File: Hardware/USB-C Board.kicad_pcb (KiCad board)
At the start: 2 copper layers, 34 x 34 mm, 52 parts, among them J1 USB_C_Receptacle_USB2.0, J2 Conn_01x04_Male, J3 Conn_01x02_Male, J4 Conn_01x02_Male, J5 Conn_01x02_Male, J9 Conn_01x04_MountingPin, Q1 DMP3013SFV, SW1 SW_Push, U1 AMS1117-3.3, U3 STUSB4500QTR

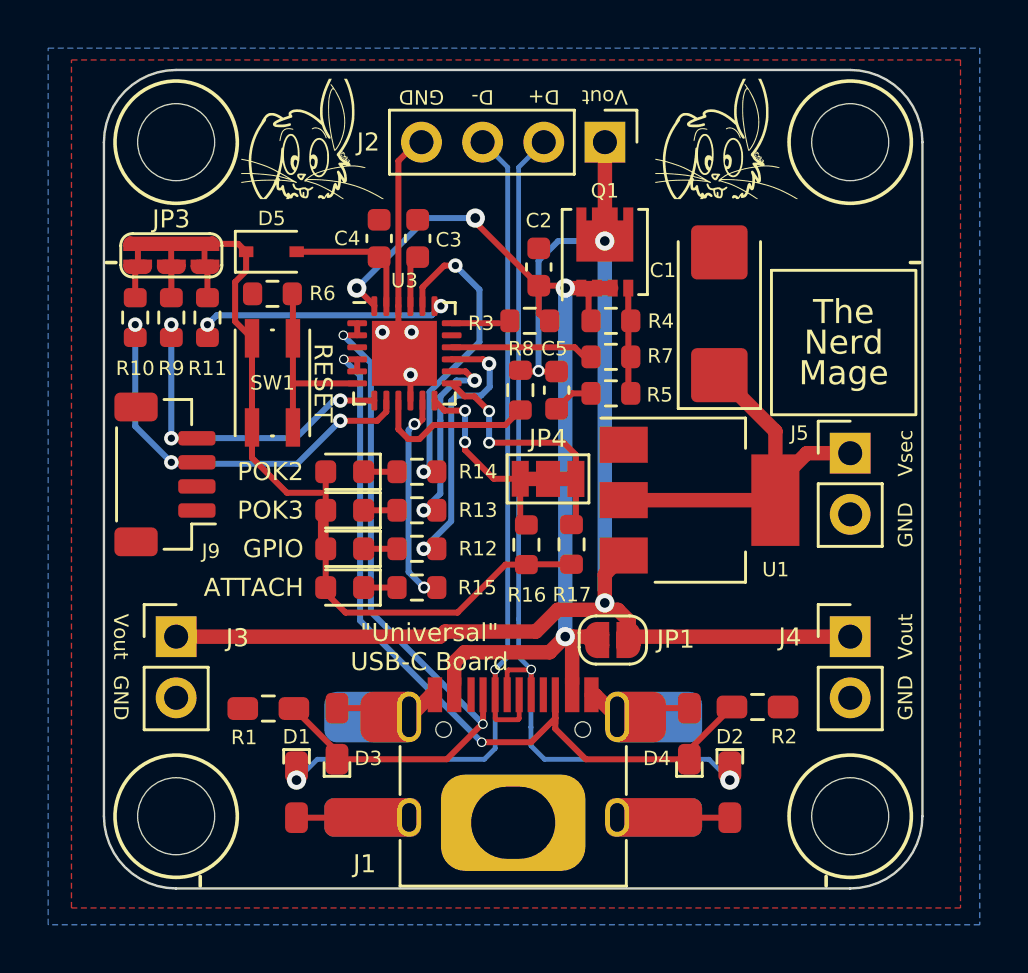
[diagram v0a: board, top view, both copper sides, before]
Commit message: tweakin' header positions
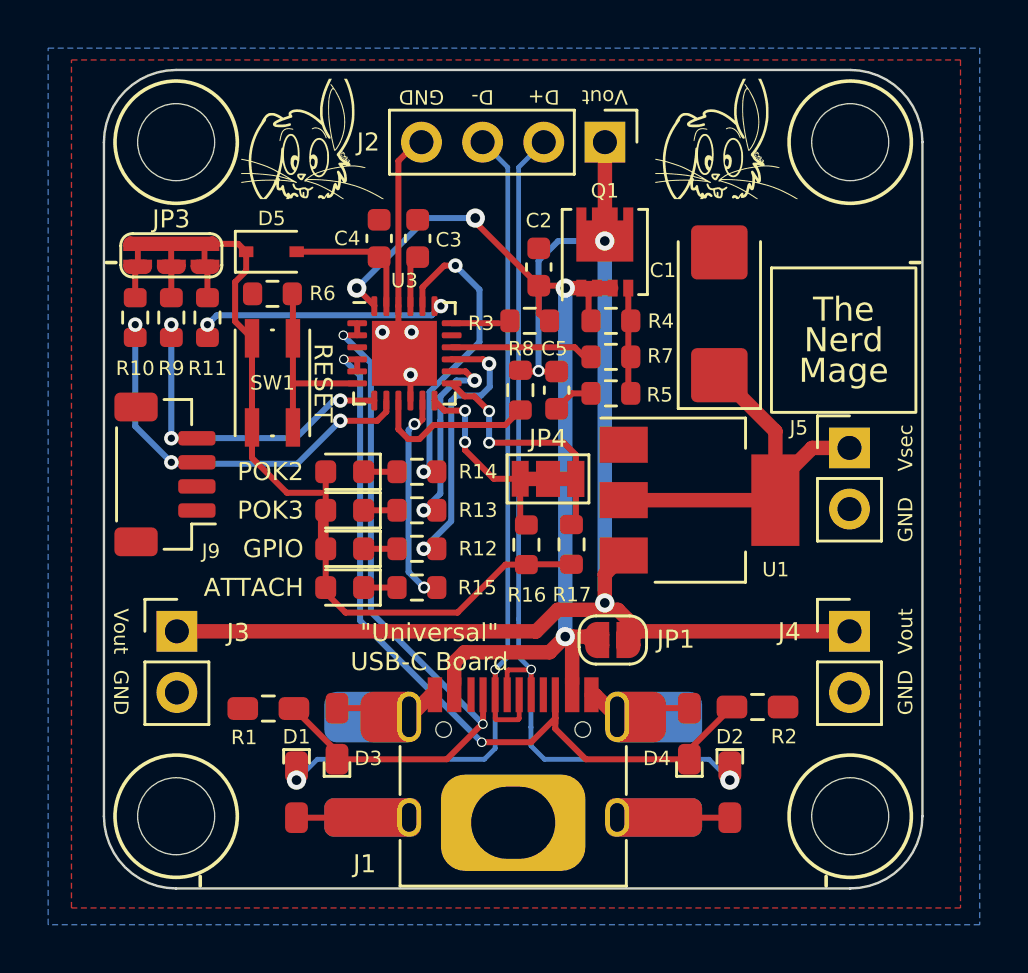
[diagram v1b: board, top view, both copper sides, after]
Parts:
- moved J3 0.22 mm to (86.0, 93.3)
- moved J4 0.22 mm to (114.0, 93.3)
- moved J5 0.22 mm to (114.0, 85.7)
- moved REF** 0.10 mm to (113.7, 81.2)
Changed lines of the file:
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@@
   )
   (footprint "Connector_PinHeader_2.54mm:PinHeader_1x02_P2.54mm_Vertical" (layer "F.Cu")
-    (at 114 93.54)
+    (at 113.97 93.32)
     (descr "Through hole straight pin header, 1x02, 2.54mm pitch, single row")
     (tags "Through hole pin header THT 1x02 2.54mm single row")
@@
   )
   (footprint "Tinker:NerdMage" (layer "F.Cu")
-    (at 113.729274 81.323075)
+    (at 113.729274 81.223075)
     (attr smd)
     (fp_text reference "REF**" (at 0 -0.5 unlocked) (layer "F.SilkS") hide
@@
   )
   (footprint "Connector_PinHeader_2.54mm:PinHeader_1x02_P2.54mm_Vertical" (layer "F.Cu")
-    (at 86 93.54)
+    (at 86.03 93.32)
     (descr "Through hole straight pin header, 1x02, 2.54mm pitch, single row")
     (tags "Through hole pin header THT 1x02 2.54mm single row")
@@
   )
   (footprint "Connector_PinHeader_2.54mm:PinHeader_1x02_P2.54mm_Vertical" (layer "F.Cu")
-    (at 114 85.92)
+    (at 113.97 85.7)
     (descr "Through hole straight pin header, 1x02, 2.54mm pitch, single row")
     (tags "Through hole pin header THT 1x02 2.54mm single row")
@@
     (effects (font (size 0.6 0.6) (thickness 0.15)) (justify mirror))
   )
-  (gr_text "GND" (at 116.3 88.9 90) (layer "B.SilkS")
+  (gr_text "GND" (at 116.3 88.68 90) (layer "B.SilkS")
     (effects (font (size 0.6 0.6) (thickness 0.125)) (justify mirror))
   )
-  (gr_text "GND" (at 83.7 96.08 270) (layer "B.SilkS")
+  (gr_text "GND" (at 83.7 95.86 270) (layer "B.SilkS")
     (effects (font (size 0.6 0.6) (thickness 0.125)) (justify mirror))
   )
-  (gr_text "Vout" (at 116.3 93.54 90) (layer "B.SilkS")
+  (gr_text "Vout" (at 116.3 93.32 90) (layer "B.SilkS")
     (effects (font (size 0.6 0.6) (thickness 0.125)) (justify mirror))
   )
@@
     (effects (font (size 0.6 0.6) (thickness 0.125)) (justify mirror))
   )
-  (gr_text "Vsec" (at 116.3 85.92 90) (layer "B.SilkS")
+  (gr_text "Vsec" (at 116.3 85.7 90) (layer "B.SilkS")
     (effects (font (size 0.6 0.6) (thickness 0.125)) (justify mirror))
   )
-  (gr_text "GND" (at 116.3 96.08 90) (layer "B.SilkS")
+  (gr_text "GND" (at 116.3 95.86 90) (layer "B.SilkS")
     (effects (font (size 0.6 0.6) (thickness 0.125)) (justify mirror))
   )
@@
     (effects (font (size 1 1) (thickness 0.15)) (justify mirror))
   )
-  (gr_text "Vout" (at 83.7 93.54 270) (layer "B.SilkS")
+  (gr_text "Vout" (at 83.7 93.32 270) (layer "B.SilkS")
     (effects (font (size 0.6 0.6) (thickness 0.125)) (justify mirror))
   )
@@
     (effects (font (size 0.6 0.6) (thickness 0.125)) (justify mirror))
   )
-  (gr_text "Vout" (at 116.3 93.54 90) (layer "F.SilkS")
+  (gr_text "Vout" (at 116.3 93.32 90) (layer "F.SilkS")
     (effects (font (size 0.6 0.6) (thickness 0.125)))
   )
@@
     (effects (font (size 0.6 0.6) (thickness 0.15)))
   )
-  (gr_text "GND" (at 116.3 88.9 90) (layer "F.SilkS")
+  (gr_text "GND" (at 116.3 88.68 90) (layer "F.SilkS")
     (effects (font (size 0.6 0.6) (thickness 0.125)))
   )
@@
     (effects (font (size 0.75 0.75) (thickness 0.15)) (justify right))
   )
-  (gr_text "GND" (at 116.3 96.08 90) (layer "F.SilkS")
+  (gr_text "GND" (at 116.3 95.86 90) (layer "F.SilkS")
     (effects (font (size 0.6 0.6) (thickness 0.125)))
   )
@@
     (effects (font (size 0.75 0.75) (thickness 0.15)) (justify right))
   )
-  (gr_text "GND" (at 83.7 96.08 270) (layer "F.SilkS")
+  (gr_text "GND" (at 83.7 95.86 270) (layer "F.SilkS")
     (effects (font (size 0.6 0.6) (thickness 0.125)))
   )
@@
     (effects (font (size 0.6 0.6) (thickness 0.125)))
   )
-  (gr_text "Vsec" (at 116.3 85.92 90) (layer "F.SilkS")
+  (gr_text "Vsec" (at 116.3 85.7 90) (layer "F.SilkS")
     (effects (font (size 0.6 0.6) (thickness 0.125)))
   )
-  (gr_text "Vout" (at 83.7 93.54 270) (layer "F.SilkS")
+  (gr_text "Vout" (at 83.7 93.32 270) (layer "F.SilkS")
     (effects (font (size 0.6 0.6) (thickness 0.125)))
   )
@@
   (segment (start 87.3 79.460136) (end 87.3 78.28) (width 0.25) (layer "F.Cu") (net 25))
   (segment (start 87.3 78.28) (end 87.2 78.18) (width 0.25) (layer "F.Cu") (net 25))
+  (segment (start 100.94 93.32) (end 100.947498 93.327498) (width 0.6) (layer "F.Cu") (net 26))
+  (segment (start 86 93.32) (end 100.94 93.32) (width 0.6) (layer "F.Cu") (net 26))
   (segment (start 101.849483 92.425514) (end 104.348538 92.425514) (width 0.6) (layer "F.Cu") (net 26))
   (segment (start 103.81 77.101582) (end 103.805361 77.106221) (width 0.6) (layer "F.Cu") (net 26))
   (segment (start 103.805361 92.14) (end 103.805361 90.956371) (width 0.6) (layer "F.Cu") (net 26))
   (segment (start 103.805361 90.956371) (end 104.591978 90.169754) (width 0.6) (layer "F.Cu") (net 26))
+  (segment (start 100.947498 93.327498) (end 101.849483 92.425514) (width 0.6) (layer "F.Cu") (net 26))
+  (segment (start 114 93.32) (end 105.243024 93.32) (width 0.6) (layer "F.Cu") (net 26))
   (segment (start 101.804435 82.525911) (end 100.350399 82.525911) (width 0.25) (layer "F.Cu") (net 26))
-  (segment (start 97.172452 93.327548) (end 100.947449 93.327548) (width 0.6) (layer "F.Cu") (net 26))
-  (segment (start 104.93 93.54) (end 104.79 93.68) (width 0.6) (layer "F.Cu") (net 26))
+  (segment (start 105.243024 93.32) (end 104.79 92.866976) (width 0.6) (layer "F.Cu") (net 26))
   (segment (start 104.79 92.866976) (end 104.79 93.68) (width 0.6) (layer "F.Cu") (net 26))
-  (segment (start 96.96 93.54) (end 97.172452 93.327548) (width 0.6) (layer "F.Cu") (net 26))
   (segment (start 103.81 73) (end 103.81 77.101582) (width 0.6) (layer "F.Cu") (net 26))
   (segment (start 100.350399 82.525911) (end 100.29898 82.474492) (width 0.25) (layer "F.Cu") (net 26))
   (segment (start 104.348538 92.425514) (end 104.79 92.866976) (width 0.6) (layer "F.Cu") (net 26))
-  (segment (start 100.947449 93.327548) (end 101.849483 92.425514) (width 0.6) (layer "F.Cu") (net 26))
   (segment (start 104.79 93.98) (end 104.79 92.966976) (width 0.6) (layer "F.Cu") (net 26))
-  (segment (start 114 93.54) (end 104.93 93.54) (width 0.6) (layer "F.Cu") (net 26))
-  (segment (start 86 93.54) (end 96.96 93.54) (width 0.6) (layer "F.Cu") (net 26))
   (via (at 103.805361 77.106221) (size 0.8) (drill 0.4) (layers "F.Cu" "B.Cu") (net 26))
   (via (at 103.805361 92.14) (size 0.8) (drill 0.4) (layers "F.Cu" "B.Cu") (net 26))
@@
   (segment (start 97.599085 78.126037) (end 98.598915 79.125867) (width 0.25) (layer "B.Cu") (net 28))
   (segment (start 95.175 91.5) (end 93.7875 91.5) (width 0.25) (layer "F.Cu") (net 29))
-  (segment (start 112.2 85.92) (end 114 85.92) (width 0.6) (layer "F.Cu") (net 30))
-  (segment (start 110.891978 87.869754) (end 110.891978 87.228022) (width 0.6) (layer "F.Cu") (net 30))
+  (segment (start 110.891978 87.228022) (end 112.42 85.7) (width 0.6) (layer "F.Cu") (net 30))
   (segment (start 108.564531 82.679109) (end 110.891978 85.006556) (width 0.6) (layer "F.Cu") (net 30))
   (segment (start 110.891978 87.869754) (end 104.591978 87.869754) (width 0.6) (layer "F.Cu") (net 30))
-  (segment (start 110.891978 87.228022) (end 112.2 85.92) (width 0.6) (layer "F.Cu") (net 30))
+  (segment (start 112.42 85.7) (end 114 85.7) (width 0.6) (layer "F.Cu") (net 30))
+  (segment (start 110.891978 87.869754) (end 110.891978 87.228022) (width 0.6) (layer "F.Cu") (net 30))
   (segment (start 110.891978 85.006556) (end 110.891978 87.869754) (width 0.6) (layer "F.Cu") (net 30))
   (segment (start 93.663126 89.890928) (end 95.250626 89.890928) (width 0.25) (layer "F.Cu") (net 31))

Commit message: footprint tweaks...
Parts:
- J2: footprint Connector_PinHeader_2.54mm:PinHeader_1x04_P2.54mm_Vertical -> Tinker:PinHeader_1x04_P2.54mm_Vertical
- J3, J4, J5: footprint Connector_PinHeader_2.54mm:PinHeader_1x02_P2.54mm_Vertical -> Tinker:PinHeader_1x02_P2.54mm_Vertical
- U1: footprint Package_TO_SOT_SMD:SOT-223-3_TabPin2 -> Tinker:SOT-223-3_TabPin2
- moved U1 0.89 mm to (108.6, 88.1), turned to 90 degrees
- moved C1 0.49 mm to (108.6, 79.6)
- moved REF** 0.07 mm to (113.8, 81.2)
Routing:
- net 3v3: track 16.8 -> 14.7 mm
- net Vout: track 60.7 -> 61.6 mm

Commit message: s'more tweakin'
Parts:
- removed the REF** at (108.6, 73.5)
- added J5: Conn_01x02_Male, Tinker:PinHeader_1x02_P2.54mm_Vertical, F.Cu at (113.9, 78.1)
- moved REF** 9.98 mm to (108.2, 72.9)
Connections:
- net 3v3 renamed Vsec
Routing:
- net Vsec: track 14.7 -> 21.9 mm

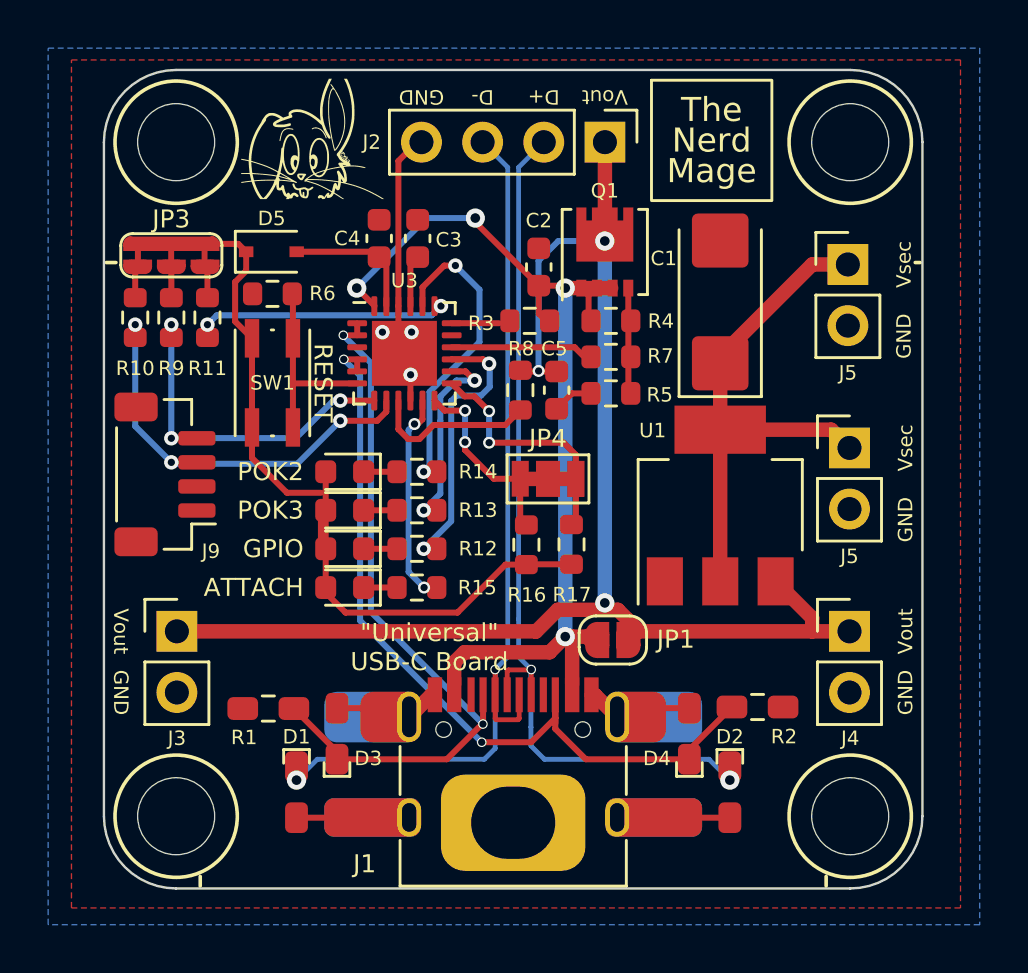
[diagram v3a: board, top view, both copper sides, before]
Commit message: Added empty controller board
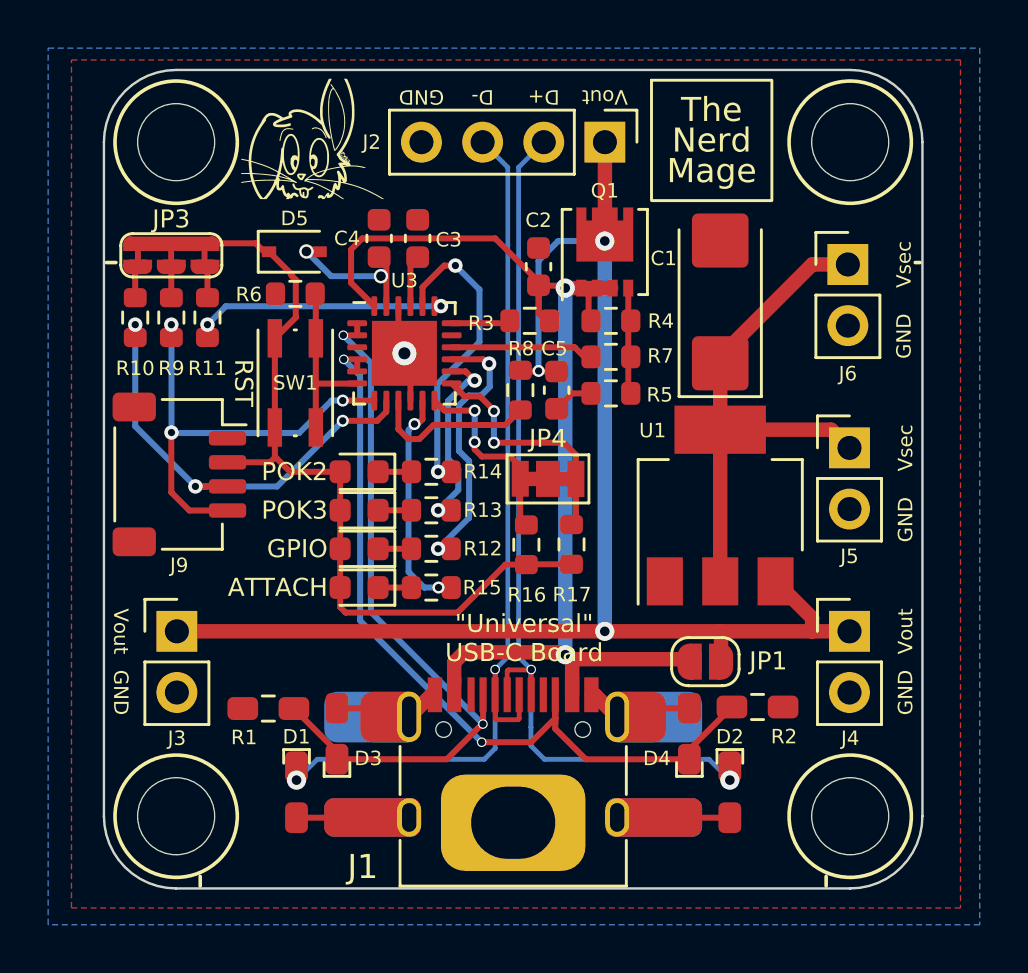
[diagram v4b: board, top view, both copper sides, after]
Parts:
- removed the J5 at (113.9, 78.1)
- added J6: Conn_01x02_Male, Tinker:PinHeader_1x02_P2.54mm_Vertical, F.Cu at (113.9, 78.1)
- J9: footprint Connector_JST:JST_SH_BM04B-SRSS-TB_1x04-1MP_P1.00mm_Vertical -> Tinker:JST_SH_SM04B-SRSS-TB_1x04-1MP_P1.00mm_Horizontal
- moved JP1 3.95 mm to (108.0, 94.6)
- moved D5 0.95 mm to (90.9, 77.6)
- moved R6 0.95 mm to (91.0, 79.3)
- moved SW1 0.95 mm to (91.0, 83.0)
- moved J9 0.60 mm to (86.1, 86.8), turned to -90 degrees
- moved D6 0.60 mm to (93.6, 89.9)
- moved D7 0.60 mm to (93.6, 88.3)
- moved D8 0.60 mm to (93.6, 86.7)
- moved D9 0.60 mm to (93.6, 91.5)
- moved R12 0.60 mm to (96.6, 89.9)
- moved R13 0.60 mm to (96.6, 88.3)
- moved R14 0.60 mm to (96.6, 86.7)
- moved R15 0.60 mm to (96.6, 91.5)
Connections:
- net ADDR0 renamed /ADDR0
- net ADDR1 renamed /ADDR1
- J9 pad 2: unconnected-(J9-Pad2) -> 2v7
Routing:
- net GND: track 25.4 -> 18.1 mm, vias 3 -> 1
- net SCL: track 13.8 -> 18.7 mm
- net Vbus: track 41.2 -> 45.6 mm, vias 4 -> 2
- net SDA: track 16.7 -> 18.9 mm
- net RESET: track 8.23 -> 7.25 mm
- net 2v7: track 33.8 -> 34.5 mm
- net ATTACH: track 8.26 -> 8.86 mm
- net Net-(C4-Pad1): track 5.67 -> 5.68 mm, vias 0 -> 2
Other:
- board text added: "RST"
- board text removed: "RESET"
